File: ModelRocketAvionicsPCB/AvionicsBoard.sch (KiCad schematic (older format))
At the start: 13 parts

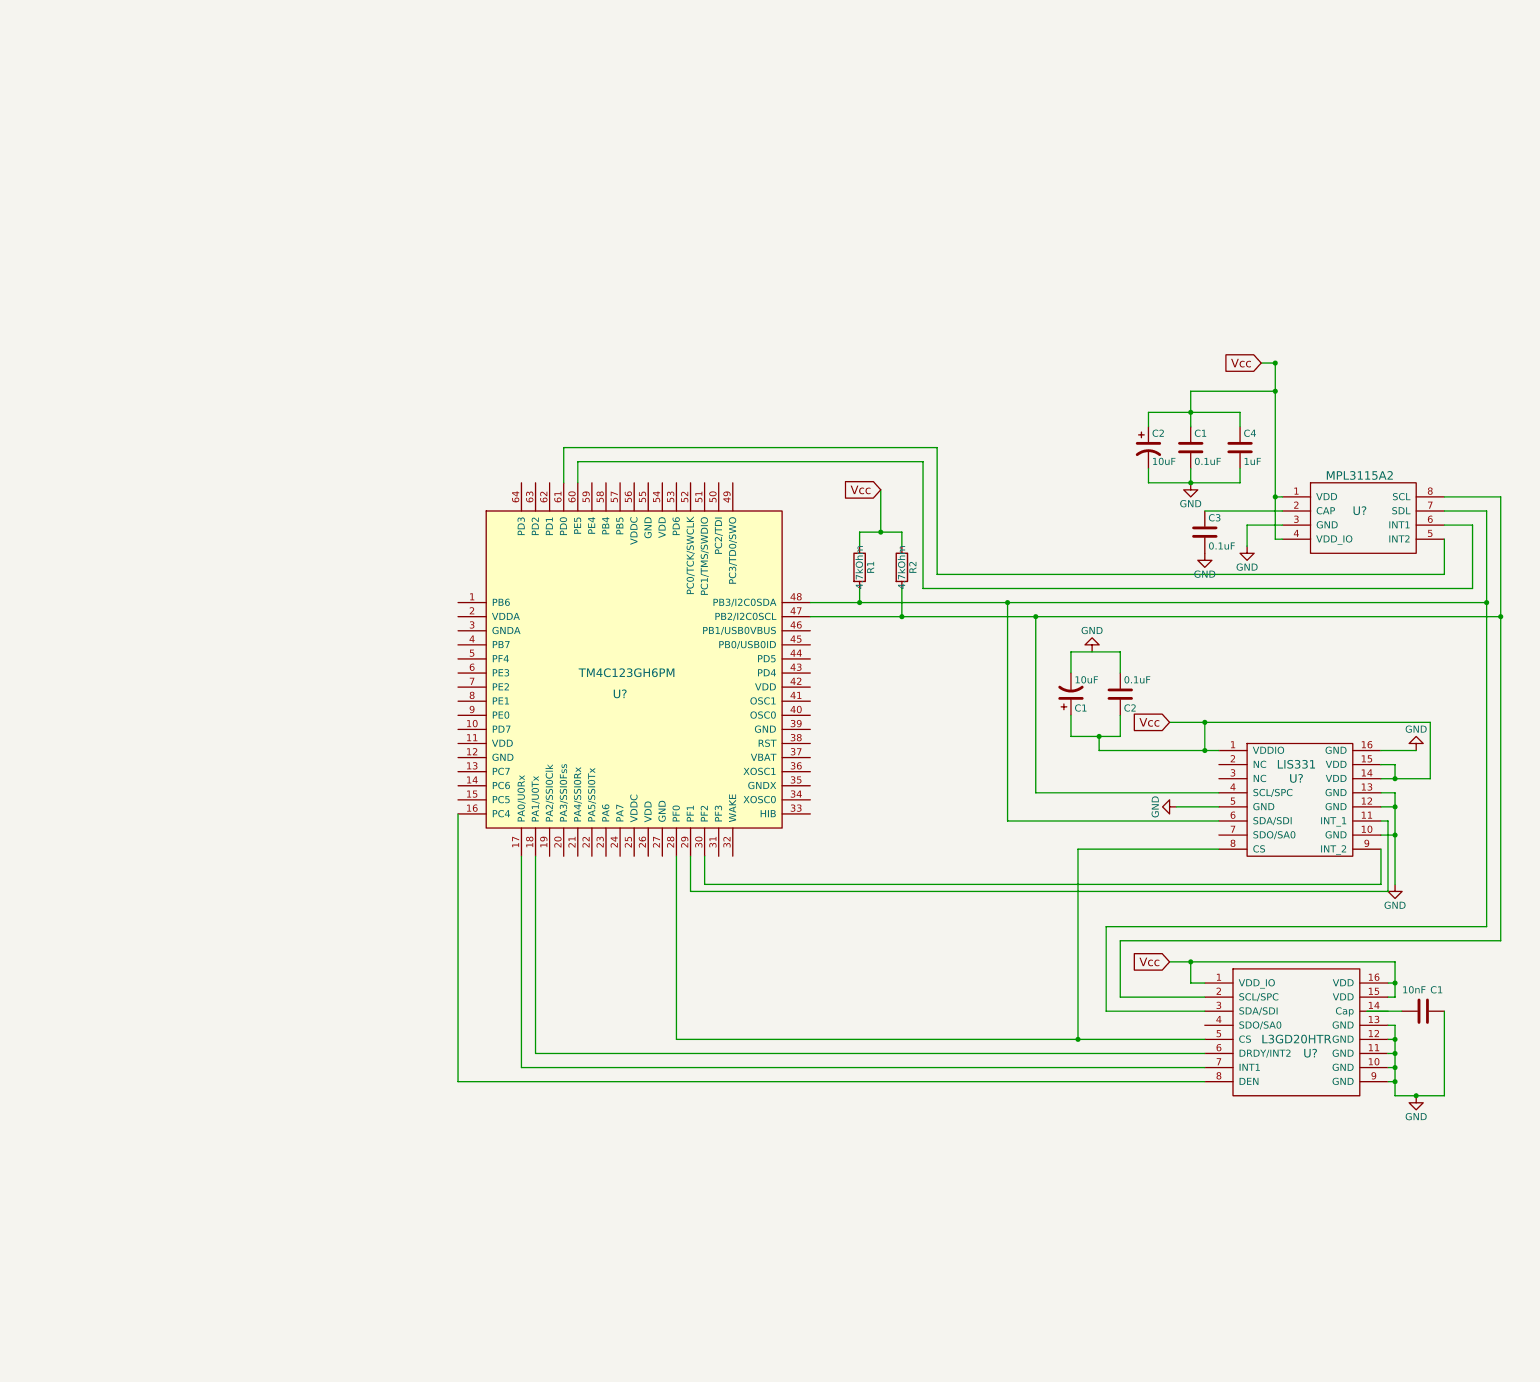
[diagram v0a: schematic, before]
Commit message: Compiled sensors on another Sheet, added uSD card/flash chip, jtag interface, power supply filter caps and started to add USB OTG
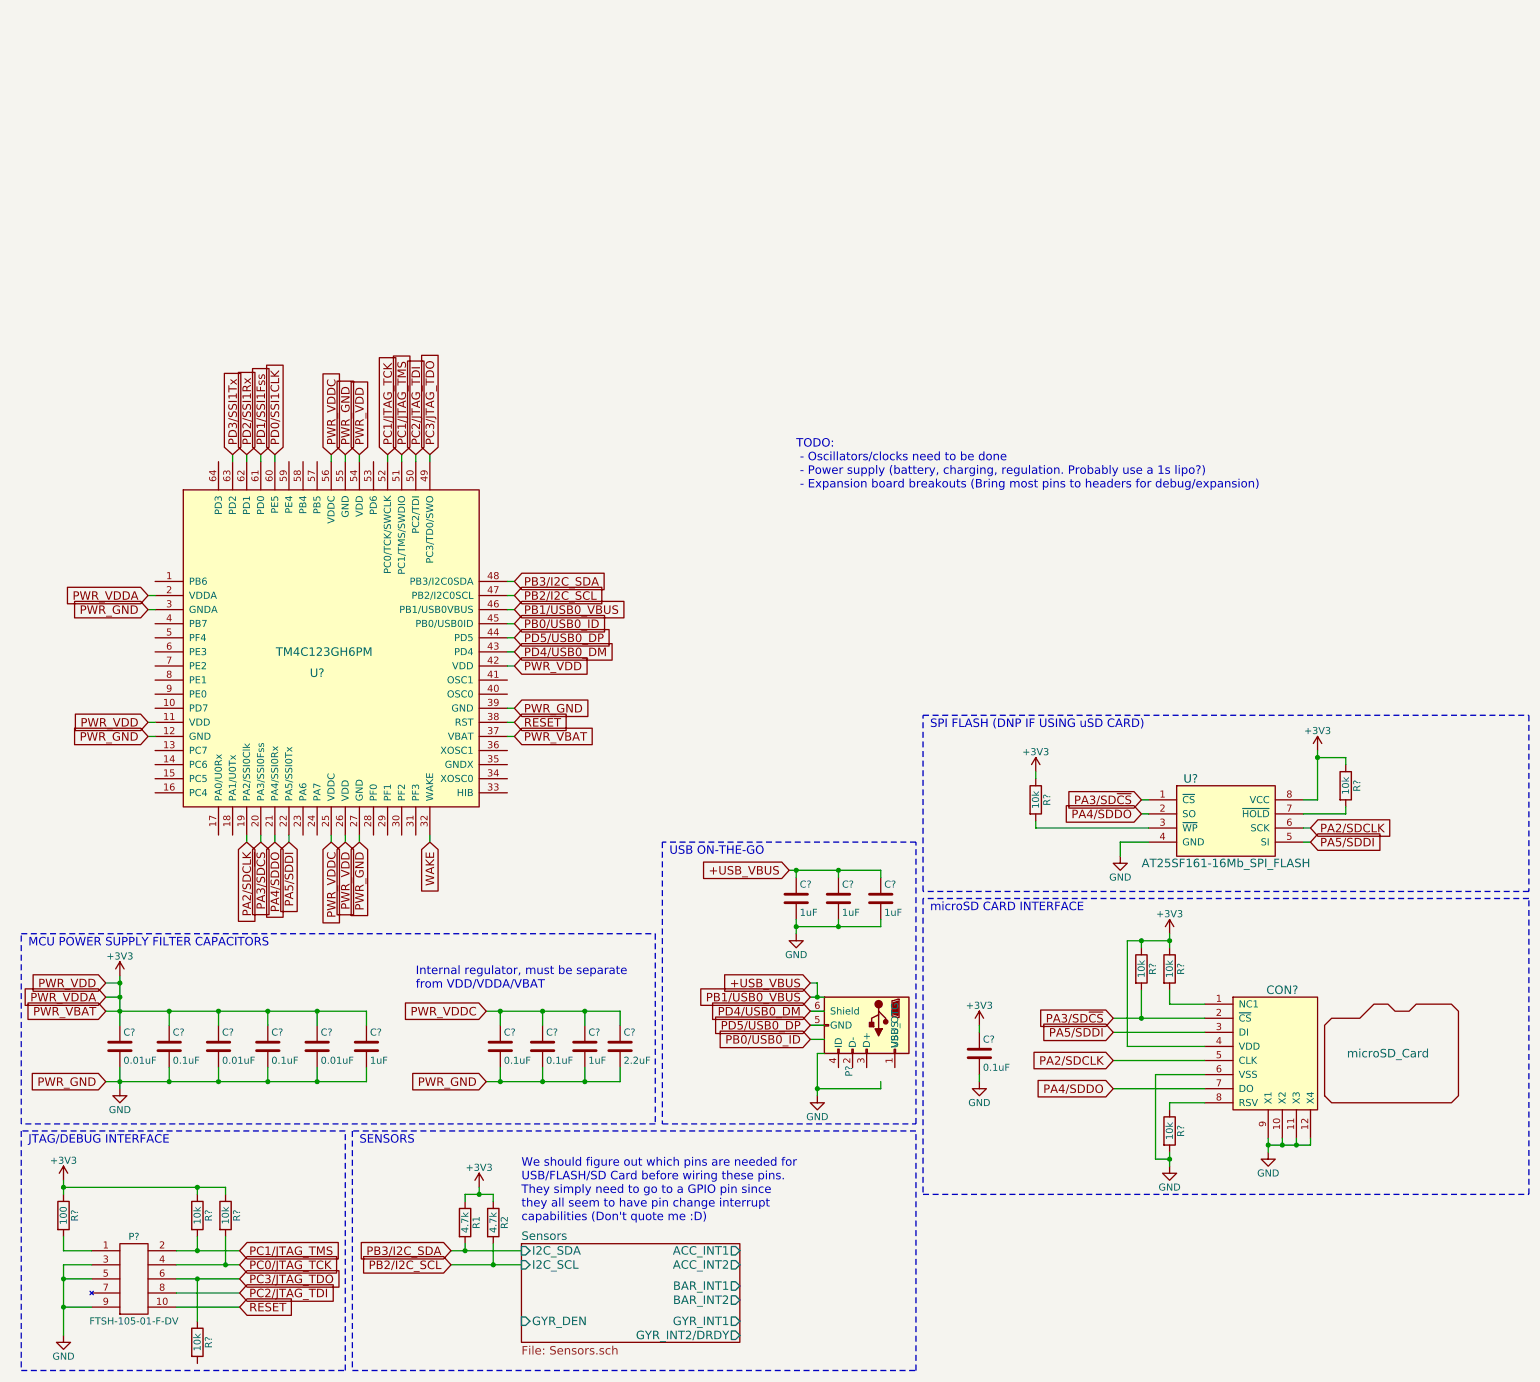
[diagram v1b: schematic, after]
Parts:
- removed C1, C2: 10uF, symbol CP1
- removed C1: 10nF, symbol C
- removed C1, C2, C3: 0.1uF, symbol C
- removed C4: 1uF, symbol C
- removed U?: LIS331, symbol LIS331
- removed U?: L3GD20HTR, symbol L3GD20HTR
- removed U?: MPL3115A2, symbol MPL3115A2
- added C? (x3): 0.01uF, symbol C
- added C? (x5): 0.1uF, symbol C
- added C? (x5): 1uF, symbol C
- added C?: 2.2uF, symbol C
- added CON?: microSD_Card, symbol microSD_Card
- added P?: FTSH-105-01-F-DV, symbol FTSH-105-01-F-DV
- added P?: USB_OTG, symbol USB_OTG
- added R?: 100, symbol R
- added R? (x8): 10k, symbol R
- added U?: AT25SF161-16Mb_SPI_FLASH, symbol AT25SF161-16Mb_SPI_FLASH
- R1, R2: value 4.7kOhm -> 4.7k
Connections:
- net labels added: +3V3, +USB_VBUS, PA2/SDCLK, PA3/SD~CS, PA4/SDDO, PA5/SDDI, PB0/USB0_ID, PB1/USB0_VBUS, PB2/I2C_SCL, PB3/I2C_SDA, PC0/JTAG_TCK, PC1/JTAG_TCK, PC1/JTAG_TMS, PC2/JTAG_TDI, PC3/JTAG_TDO, PD0/SSI1CLK, PD1/SSI1Fss, PD2/SSI1Rx, PD3/SSI1Tx, PD4/USB0_DM, PD5/USB0_DP, PWR_GND, PWR_VBAT, PWR_VDD, PWR_VDDA, PWR_VDDC, RESET, WAKE
- net labels removed: Vcc
- wire segments 101 -> 187
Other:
- note added: "Internal regulator, must be separate\nfrom VDD/VDDA/VBAT"
- note added: "JTAG/DEBUG INTERFACE"
- note added: "MCU POWER SUPPLY FILTER CAPACITORS"
- note added: "SENSORS"
- note added: "SPI FLASH (DNP IF USING uSD CARD)"
- note added: "TODO:\n - Oscillators/clocks need to be done\n - Power supply (battery, charging, regulation. Probably use a 1s lipo?)\n - Expansion board breakouts (Bring most pins to headers for debug/expansion)\n"
- note added: "USB ON-THE-GO"
- note added: "We should figure out which pins are needed for \nUSB/FLASH/SD Card before wiring these pins. \nThey simply need to go to a GPIO pin since \nthey all seem to have pin change interrupt \ncapabilities (Don't quote me :D)"
- note added: "microSD CARD INTERFACE"
- moved on the sheet: R1, R2, U?

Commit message: Added oscillators and reset button/circuit
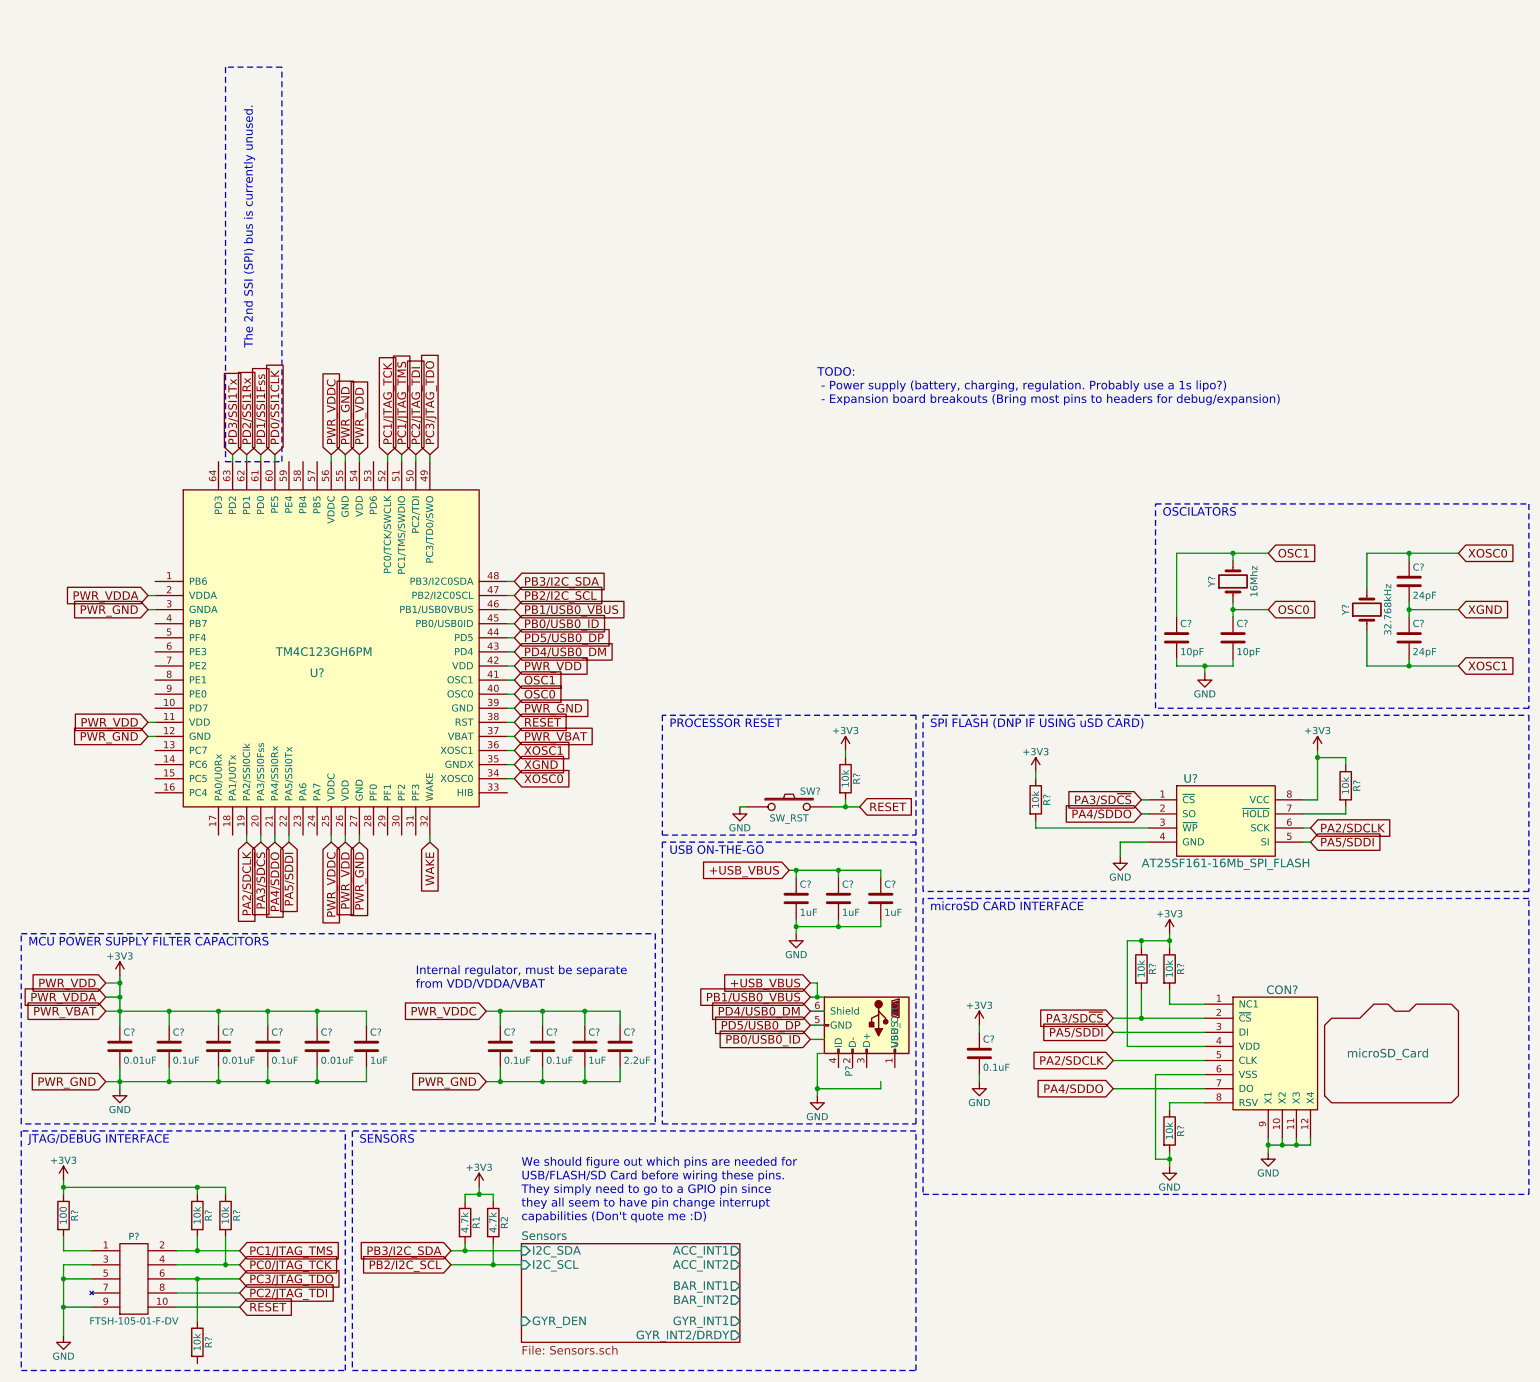
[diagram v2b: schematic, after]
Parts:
- added C? (x2): 10pF, symbol C
- added C? (x2): 24pF, symbol C
- added R?: 10k, symbol R
- added SW?: SW_RST, symbol SW_PUSH
- added Y?: 16Mhz, symbol Crystal
- added Y?: 32.768kHz, symbol Crystal
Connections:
- net labels added: OSC0, OSC1, XGND, XOSC0, XOSC1
- wire segments 187 -> 220
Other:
- note added: "OSCILATORS"
- note added: "PROCESSOR RESET"
- note added: "TODO:\n - Power supply (battery, charging, regulation. Probably use a 1s lipo?)\n - Expansion board breakouts (Bring most pins to headers for debug/expansion)\n"
- note added: "The 2nd SSI (SPI) bus is currently unused."
- note removed: "TODO:\n - Oscillators/clocks need to be done\n - Power supply (battery, charging, regulation. Probably use a 1s lipo?)\n - Expansion board breakouts (Bring most pins to headers for debug/expansion)\n"
